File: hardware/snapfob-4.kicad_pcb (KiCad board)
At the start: 2 copper layers, 26.5 x 57.3 mm, 8 parts, among them SW1 SW1, SW2 SW2, SW3 SW3, SW4 SW4, U1 SM200

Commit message: First attempt at routing.
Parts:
- U1: value SM200 -> SM220
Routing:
- net +3.3V: track 0.00 -> 69.7 mm
- net GND: track 0.00 -> 31.7 mm, vias 0 -> 5
- net Net-(SW1-Pad1): track 0.00 -> 22.1 mm, vias 0 -> 1
- net Net-(SW2-Pad1): track 0.00 -> 20.4 mm, vias 0 -> 1
- net Net-(SW4-Pad1): track 0.00 -> 7.97 mm, vias 0 -> 1
- net Net-(SW3-Pad1): track 0.00 -> 3.31 mm, vias 0 -> 1
- added copper zone on B.Cu, net GND
- added copper zone on F.Cu, net GND
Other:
- net class VCC added: clearance 0.254, trace_width 0.762, via_dia 0.889, via_drill 0.635
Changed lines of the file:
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@@
   (general
     (links 29)
-    (no_connects 29)
-    (area 0 0 0 0)
+    (no_connects 4)
+    (area 124.434686 50.371 161.9774 109.064)
     (thickness 1.6)
     (drawings 5)
-    (tracks 0)
+    (tracks 59)
     (zones 0)
     (modules 8)
@@
   (layers
     (0 F.Cu signal)
-    (31 B.Cu signal hide)
-    (32 B.Adhes user hide)
+    (31 B.Cu signal)
+    (32 B.Adhes user)
     (33 F.Adhes user)
-    (34 B.Paste user hide)
+    (34 B.Paste user)
     (35 F.Paste user)
-    (36 B.SilkS user hide)
-    (37 F.SilkS user)
-    (38 B.Mask user hide)
+    (36 B.SilkS user)
+    (37 F.SilkS user hide)
+    (38 B.Mask user)
     (39 F.Mask user)
     (40 Dwgs.User user)
@@
     (46 B.CrtYd user)
     (47 F.CrtYd user)
-    (48 B.Fab user hide)
+    (48 B.Fab user)
     (49 F.Fab user)
   )
@@
     (pad_to_mask_clearance 0)
     (aux_axis_origin 0 0)
-    (visible_elements FFFFFB7F)
+    (visible_elements FFFFFF7F)
     (pcbplotparams
-      (layerselection 0x00030_80000001)
+      (layerselection 0x01030_80000001)
       (usegerberextensions false)
       (excludeedgelayer true)
@@
       (padsonsilk false)
       (subtractmaskfromsilk false)
-      (outputformat 1)
+      (outputformat 4)
       (mirror false)
-      (drillshape 1)
+      (drillshape 0)
       (scaleselection 1)
-      (outputdirectory ""))
+      (outputdirectory outputs/))
   )
   (net 0 "")
@@
     (uvia_dia 0.508)
     (uvia_drill 0.127)
-    (add_net +3.3V)
     (add_net GND)
     (add_net "Net-(SW1-Pad1)")
@@
     (add_net "Net-(U1-PadH6)")
   )
+  (net_class VCC ""
+    (clearance 0.254)
+    (trace_width 0.762)
+    (via_dia 0.889)
+    (via_drill 0.635)
+    (uvia_dia 0.508)
+    (uvia_drill 0.127)
+    (add_net +3.3V)
+  )
   (module _CrumpPrints:CR2032_HOLDER (layer B.Cu)
     (at 142.125 97.875)
     (descr http://www.mouser.com/ds/2/238/bat-hld-001-220194.pdf)
     (tags "Linx Battery Holder 2032 bat-hld-001")
-    (fp_text reference BT1 (at 0 -10.16) (layer B.SilkS)
+    (fp_text reference BT1 (at 0 -10.16) (layer B.SilkS) hide
       (effects (font (size 1 1) (thickness 0.15)) (justify mirror))
     )
-    (fp_text value BATTERY (at 0 10.16) (layer B.SilkS)
+    (fp_text value BATTERY (at 0 10.16) (layer B.SilkS) hide
       (effects (font (size 1 1) (thickness 0.15)) (justify mirror))
     )
@@
       (effects (font (size 1.2 1.2) (thickness 0.2)) (justify mirror))
     )
-    (fp_text value SM200 (at 6.35 -11.43 180) (layer B.SilkS)
+    (fp_text value SM220 (at 6.35 -11.43 180) (layer B.SilkS)
       (effects (font (size 1.2 1.2) (thickness 0.2)) (justify mirror))
     )
@@
     (effects (font (size 1.5 1.5) (thickness 0.3)))
   )
+  (segment (start 134.25 85.845) (end 149.5 85.845) (width 0.762) (layer B.Cu) (net 1))
+  (segment (start 149.5 85.845) (end 150 87.25) (width 0.762) (layer B.Cu) (net 1))
+  (segment (start 150.525 72.175) (end 150.675 72.175) (width 0.762) (layer B.Cu) (net 1))
+  (segment (start 150.675 72.175) (end 152 73.5) (width 0.762) (layer B.Cu) (net 1))
+  (segment (start 152 85.25) (end 150 87.25) (width 0.762) (layer B.Cu) (net 1))
+  (segment (start 152 73.5) (end 152 85.25) (width 0.762) (layer B.Cu) (net 1))
+  (segment (start 150 87.25) (end 150 90.5) (width 0.762) (layer B.Cu) (net 1))
+  (segment (start 153.575 94.075) (end 153.575 97.875) (width 0.762) (layer B.Cu) (net 1))
+  (segment (start 150 90.5) (end 153.575 94.075) (width 0.762) (layer B.Cu) (net 1))
+  (segment (start 133.725 79.375) (end 133.725 76.975) (width 0.762) (layer B.Cu) (net 1))
+  (segment (start 130.675 97.875) (end 130.675 93.075) (width 0.762) (layer B.Cu) (net 1))
+  (segment (start 131.75 81.35) (end 133.725 79.375) (width 0.762) (layer B.Cu) (net 1))
+  (segment (start 131.75 83.25) (end 131.75 81.35) (width 0.762) (layer B.Cu) (net 1))
+  (segment (start 134.25 85.75) (end 131.75 83.25) (width 0.762) (layer B.Cu) (net 1))
+  (segment (start 134.25 89.5) (end 134.25 85.845) (width 0.762) (layer B.Cu) (net 1))
+  (segment (start 134.25 85.845) (end 134.25 85.75) (width 0.762) (layer B.Cu) (net 1))
+  (segment (start 130.675 93.075) (end 134.25 89.5) (width 0.762) (layer B.Cu) (net 1))
+  (segment (start 146.675 58.355) (end 146.675 60.315) (width 0.254) (layer F.Cu) (net 2))
+  (segment (start 146.675 60.315) (end 146.685 60.325) (width 0.254) (layer F.Cu) (net 2))
+  (segment (start 137.575 58.355) (end 137.575 60.105) (width 0.254) (layer F.Cu) (net 2))
+  (segment (start 137.575 60.105) (end 137.795 60.325) (width 0.254) (layer F.Cu) (net 2))
+  (segment (start 137.575 67.355) (end 136.57 67.355) (width 0.254) (layer F.Cu) (net 2))
+  (segment (start 136.57 67.355) (end 135.255 66.04) (width 0.254) (layer F.Cu) (net 2))
+  (via (at 135.255 66.04) (size 0.889) (layers F.Cu B.Cu) (net 2))
+  (segment (start 142.125 97.875) (end 142.125 97.905) (width 0.254) (layer B.Cu) (net 2))
+  (segment (start 142.125 97.905) (end 134.62 105.41) (width 0.254) (layer B.Cu) (net 2))
+  (via (at 134.62 105.41) (size 0.889) (layers F.Cu B.Cu) (net 2))
+  (segment (start 142.125 97.875) (end 142.325 97.875) (width 0.254) (layer B.Cu) (net 2))
+  (segment (start 142.325 97.875) (end 149.86 105.41) (width 0.254) (layer B.Cu) (net 2))
+  (via (at 149.86 105.41) (size 0.889) (layers F.Cu B.Cu) (net 2))
+  (segment (start 146.675 85.355) (end 146.95 84.085) (width 0.254) (layer F.Cu) (net 2) (status 400000))
+  (via (at 146.685 83.82) (size 0.889) (layers F.Cu B.Cu) (net 2))
+  (segment (start 146.95 84.085) (end 146.685 83.82) (width 0.254) (layer F.Cu) (net 2))
+  (segment (start 137.575 85.355) (end 137.53 84.085) (width 0.254) (layer F.Cu) (net 2) (status 400000))
+  (via (at 137.795 83.82) (size 0.889) (layers F.Cu B.Cu) (net 2))
+  (segment (start 137.53 84.085) (end 137.795 83.82) (width 0.254) (layer F.Cu) (net 2))
+  (segment (start 146.675 53.895) (end 146.355 53.895) (width 0.254) (layer F.Cu) (net 3))
+  (segment (start 146.355 53.895) (end 144.75 55.5) (width 0.254) (layer F.Cu) (net 3))
+  (segment (start 144.75 55.5) (end 144.75 73.5) (width 0.254) (layer F.Cu) (net 3))
+  (via (at 144.75 73.5) (size 0.889) (layers F.Cu B.Cu) (net 3))
+  (segment (start 144.75 73.5) (end 145.725 74.475) (width 0.254) (layer B.Cu) (net 3))
+  (segment (start 145.725 74.475) (end 145.725 74.575) (width 0.254) (layer B.Cu) (net 3))
+  (segment (start 137.575 62.895) (end 142.645 62.895) (width 0.254) (layer F.Cu) (net 4))
+  (segment (start 144.5 75.75) (end 145.725 76.975) (width 0.254) (layer B.Cu) (net 4))
+  (via (at 144.5 75.75) (size 0.889) (layers F.Cu B.Cu) (net 4))
+  (segment (start 143.25 74.5) (end 144.5 75.75) (width 0.254) (layer F.Cu) (net 4))
+  (segment (start 143.25 63.5) (end 143.25 74.5) (width 0.254) (layer F.Cu) (net 4))
+  (segment (start 142.645 62.895) (end 143.25 63.5) (width 0.254) (layer F.Cu) (net 4))
+  (segment (start 146.675 71.895) (end 146.675 73.175) (width 0.254) (layer F.Cu) (net 5))
+  (segment (start 147 73.5) (end 148.075 74.575) (width 0.254) (layer B.Cu) (net 5))
+  (via (at 147 73.5) (size 0.889) (layers F.Cu B.Cu) (net 5))
+  (segment (start 146.675 73.175) (end 147 73.5) (width 0.254) (layer F.Cu) (net 5))
+  (segment (start 148.075 74.575) (end 148.125 74.575) (width 0.254) (layer B.Cu) (net 5))
+  (segment (start 146.675 80.895) (end 146.675 80.825) (width 0.254) (layer F.Cu) (net 6))
+  (segment (start 146.675 80.825) (end 149.25 78.25) (width 0.254) (layer F.Cu) (net 6))
+  (segment (start 149.25 78.25) (end 149.25 75.75) (width 0.254) (layer F.Cu) (net 6))
+  (via (at 149.25 75.75) (size 0.889) (layers F.Cu B.Cu) (net 6))
+  (segment (start 149.25 75.75) (end 150.425 74.575) (width 0.254) (layer B.Cu) (net 6))
+  (segment (start 150.425 74.575) (end 150.525 74.575) (width 0.254) (layer B.Cu) (net 6))
+  (zone (net 2) (net_name GND) (layer F.Cu) (hatch edge 0.508)
+    (connect_pads (clearance 0.508))
+    (min_thickness 0.254)
+    (fill yes (arc_segments 16) (thermal_gap 0.508) (thermal_bridge_width 0.508))
+    (polygon
+      (pts
+        (xy 129.54 59.69) (xy 154.94 59.69) (xy 153.67 90.17) (xy 153.67 102.87) (xy 151.13 106.68)
+        (xy 133.35 106.68) (xy 130.81 102.87) (xy 130.81 90.17) (xy 129.54 59.69)
+      )
+    )
+  )
+  (zone (net 2) (net_name GND) (layer B.Cu) (hatch edge 0.508)
+    (connect_pads (clearance 0.508))
+    (min_thickness 0.254)
+    (fill yes (arc_segments 16) (thermal_gap 0.508) (thermal_bridge_width 0.508))
+    (polygon
+      (pts
+        (xy 129.54 59.69) (xy 154.94 59.69) (xy 153.67 90.17) (xy 153.67 102.87) (xy 151.13 106.68)
+        (xy 133.35 106.68) (xy 130.81 102.87) (xy 130.81 90.17) (xy 129.54 59.69)
+      )
+    )
+  )
 )

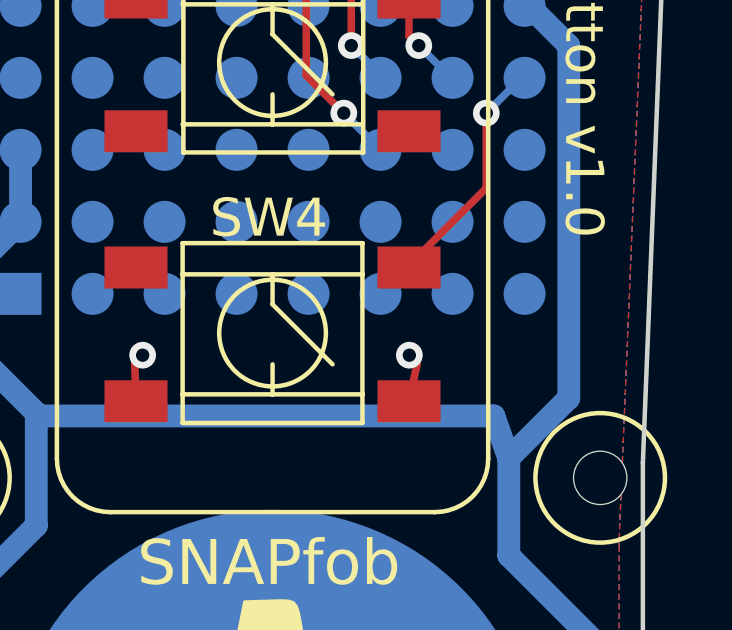
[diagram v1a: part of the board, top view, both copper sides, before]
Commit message: Pull CLKI low per datasheet.
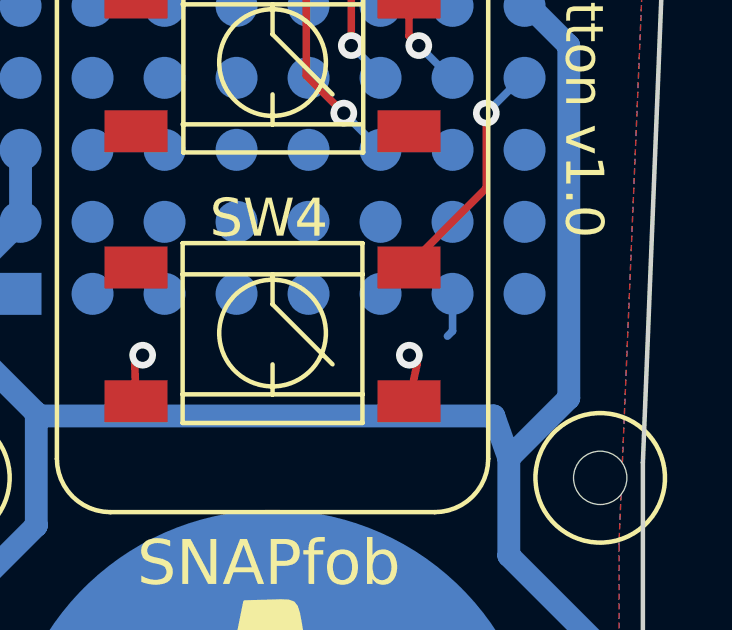
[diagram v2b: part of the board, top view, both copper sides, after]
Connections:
- U1 pad G1: Net-(U1-PadG1) -> GND
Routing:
- net GND: track 31.7 -> 33.2 mm

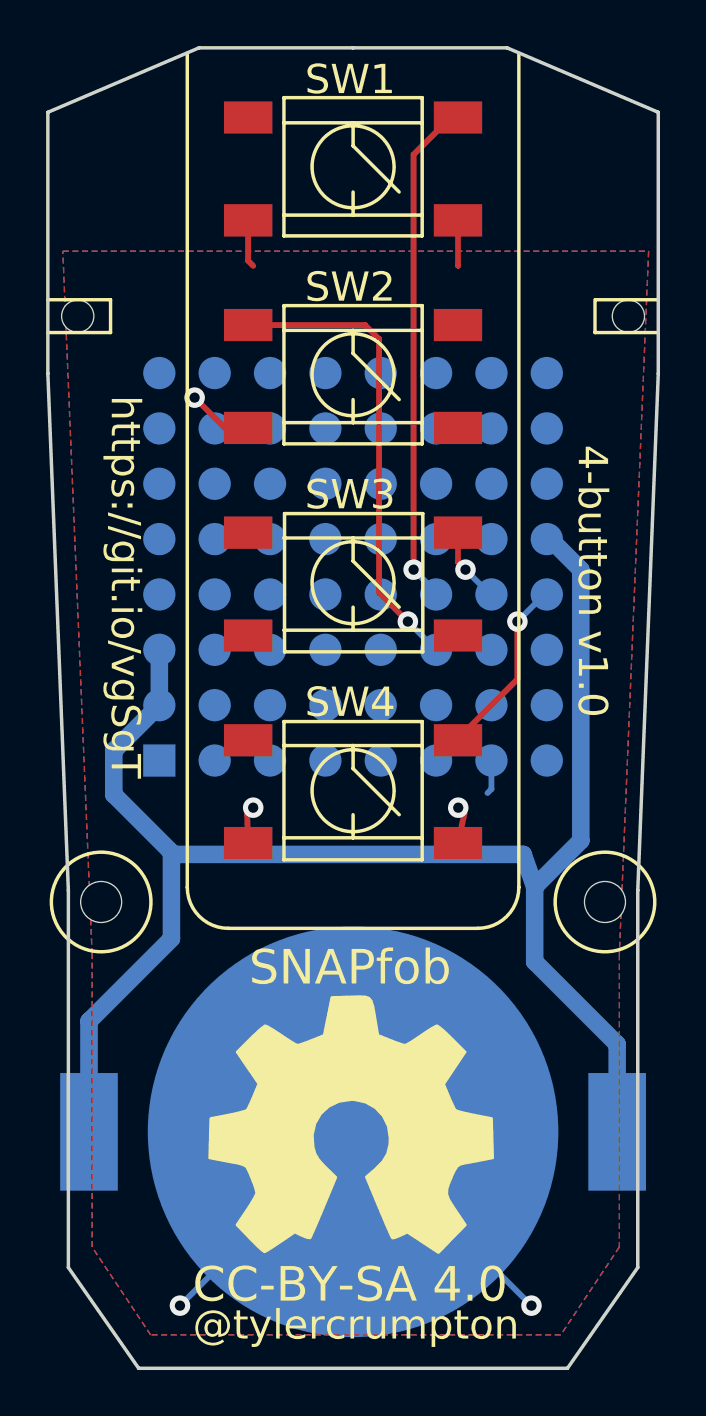
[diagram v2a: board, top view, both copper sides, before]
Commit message: Add some silk for IO designations.
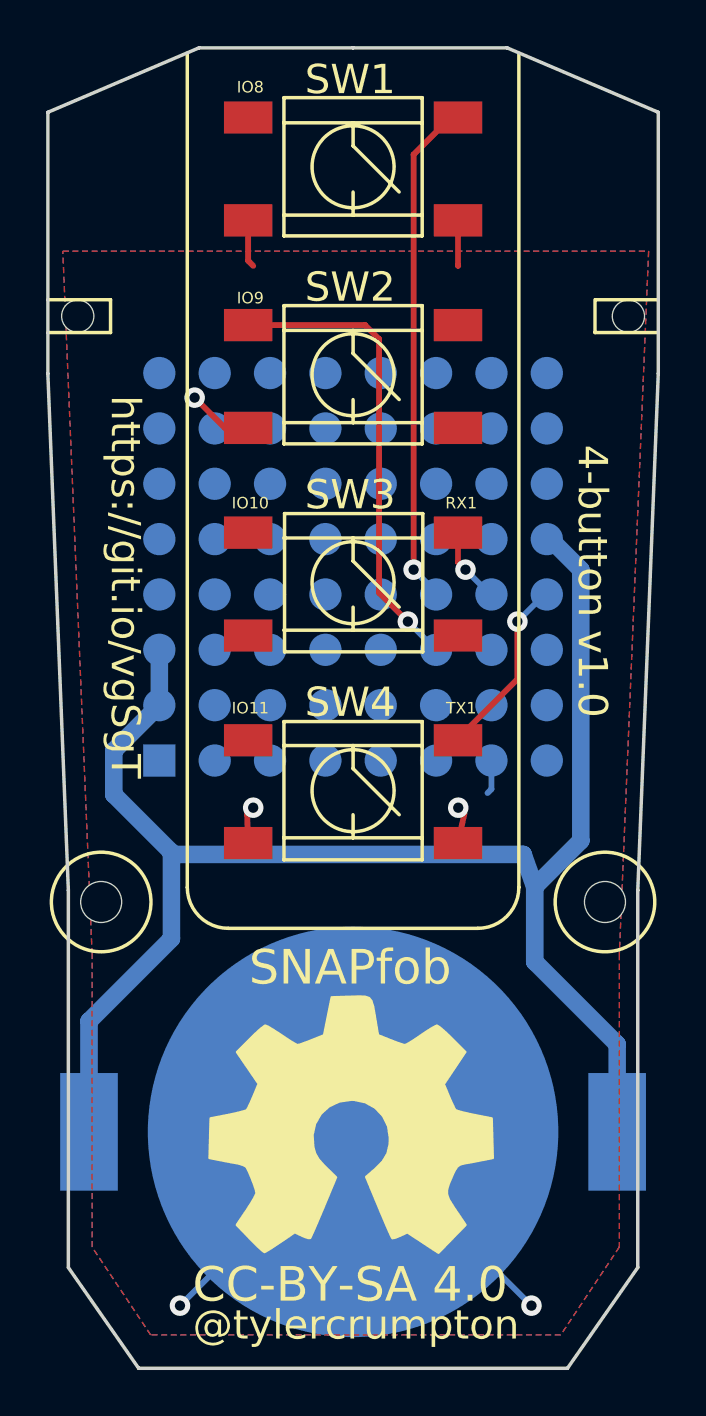
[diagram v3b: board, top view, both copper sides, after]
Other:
- board text added: "IO10"
- board text added: "IO11"
- board text added: "IO8"
- board text added: "IO9"
- board text added: "RX1"
- board text added: "TX1"
